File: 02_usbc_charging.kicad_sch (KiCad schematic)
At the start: 13 parts, among them J3 USB4105-GF-A (plating/stake l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, U2 TPS25751DREFR (active replace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, U3 BQ25792RQMR

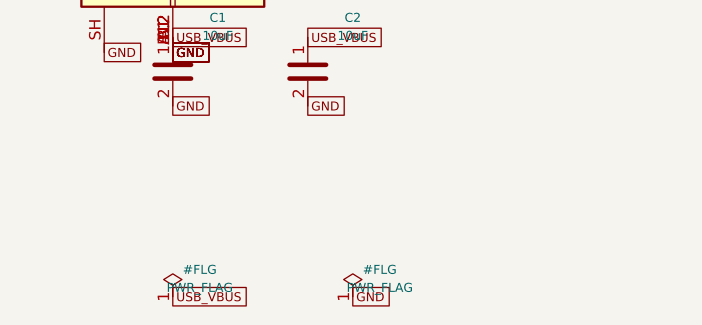
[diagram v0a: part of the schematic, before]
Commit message: Root sheet + full-hierarchy fixes (PWR_FLAG uniqueness, annotation, D-designator collision)
- red-light-panel.kicad_sch: 7 sheet symbols, no sheet-pins (global-label
  connectivity throughout, see docs/design_notes.md).
- tools/kicad_gen/fix_instance_paths.py: one-time pass populating each
  sub-sheet's per-symbol instances block with the real root-relative path
  (kicad-cli sch upgrade was silently emptying these -- invisible to ERC,
  but kicad-cli sch export bom flagged it as an annotation error).
- Fixed: multiple PWR_FLAGs on the same merged net conflicting with each
  other at full-hierarchy scale (now exactly one per net, project-wide);
  duplicate unnumbered '#FLG' references across sheets; a real
  reference-designator collision in the original BOM itself (D5-D68 LED
  range numerically includes D6/D7/D8, reused for sheet 6/7 parts --
  renumbered those three to D69/D70/D71).

Full-hierarchy 'kicad-cli sch erc' on the root sheet: 0 errors (157
cosmetic endpoint-off-grid warnings, 3 expected lib_symbol_mismatch
warnings from flattened extends-based parts). 'kicad-cli sch export bom':
153 rows, zero blank footprints, zero duplicate references, no
annotation warning.

Co-Authored-By: Claude Sonnet 5 <noreply@anthropic.com>
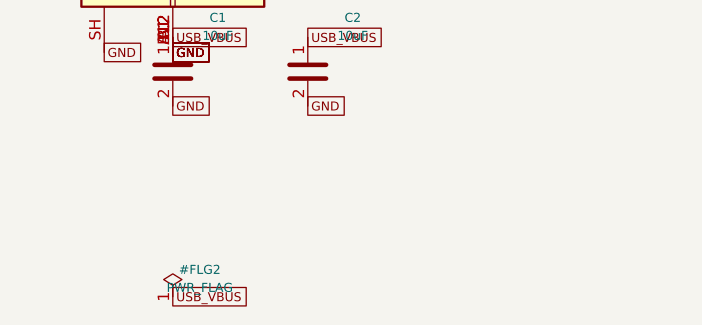
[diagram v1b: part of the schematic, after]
